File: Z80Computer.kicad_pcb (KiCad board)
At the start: 2 copper layers, 152.4 x 129.5 mm, 38 parts, among them IC1 Z80CPU, IC2_EEPROM1 28C256, IC6_SRAM1 KM62256CLP, J1 Conn_Coaxial_Power, J2 Conn_01x08_Pin, J3 Conn_01x08_Pin, SW1 SW_Push, U1 74LS244, U2 74LS32, U3 74LS273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

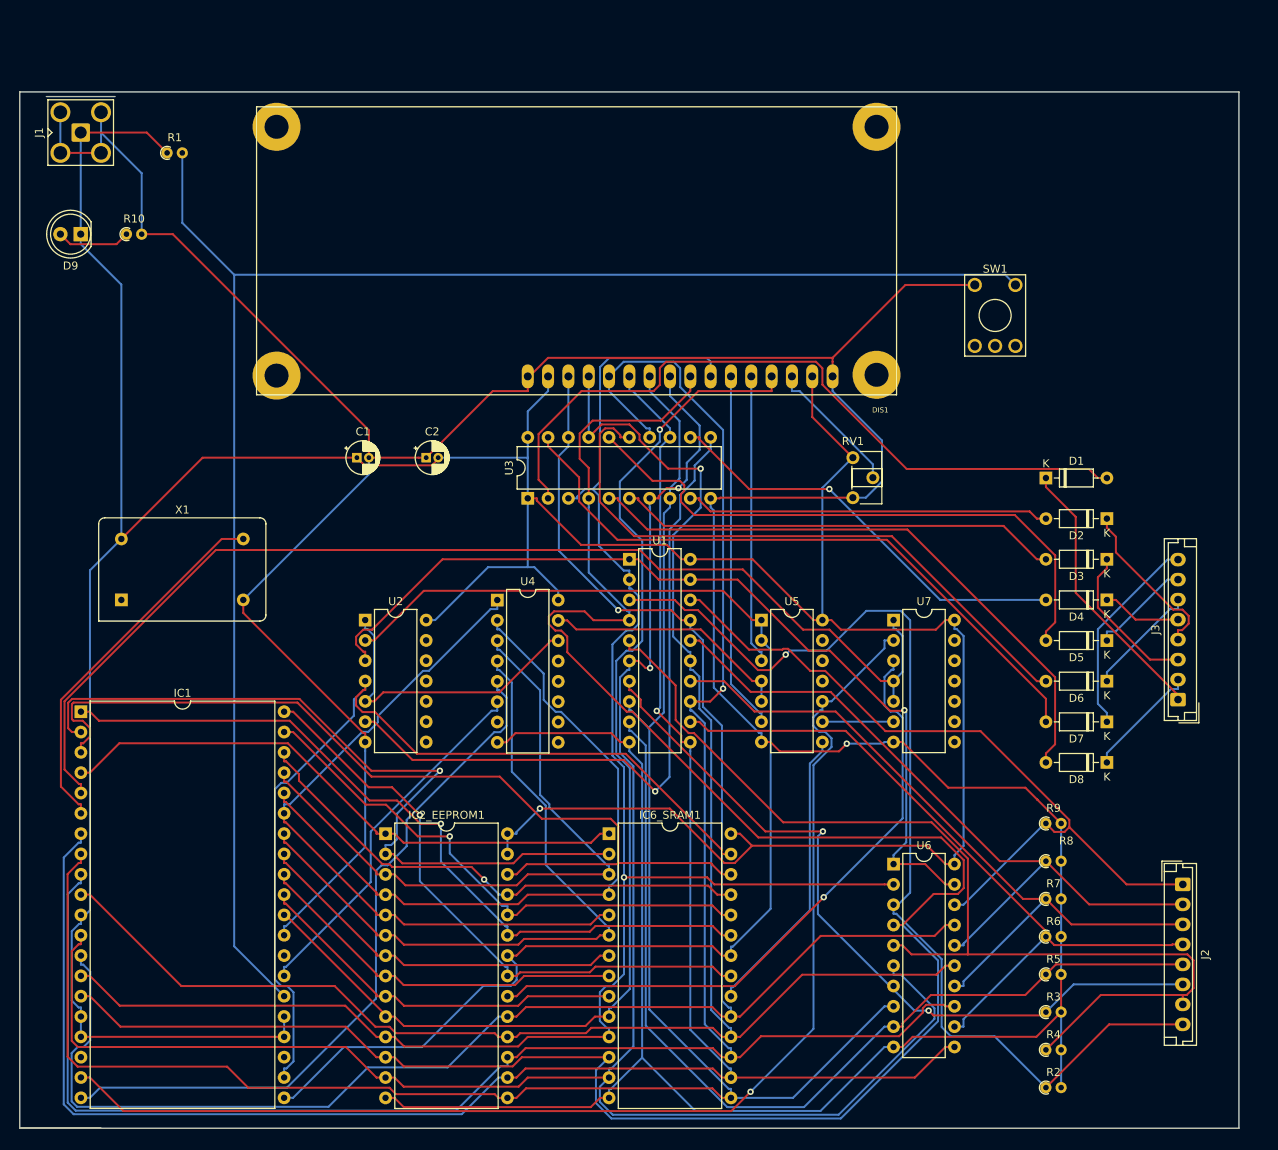
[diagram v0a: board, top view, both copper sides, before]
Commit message: reworked to correct z80 footprint
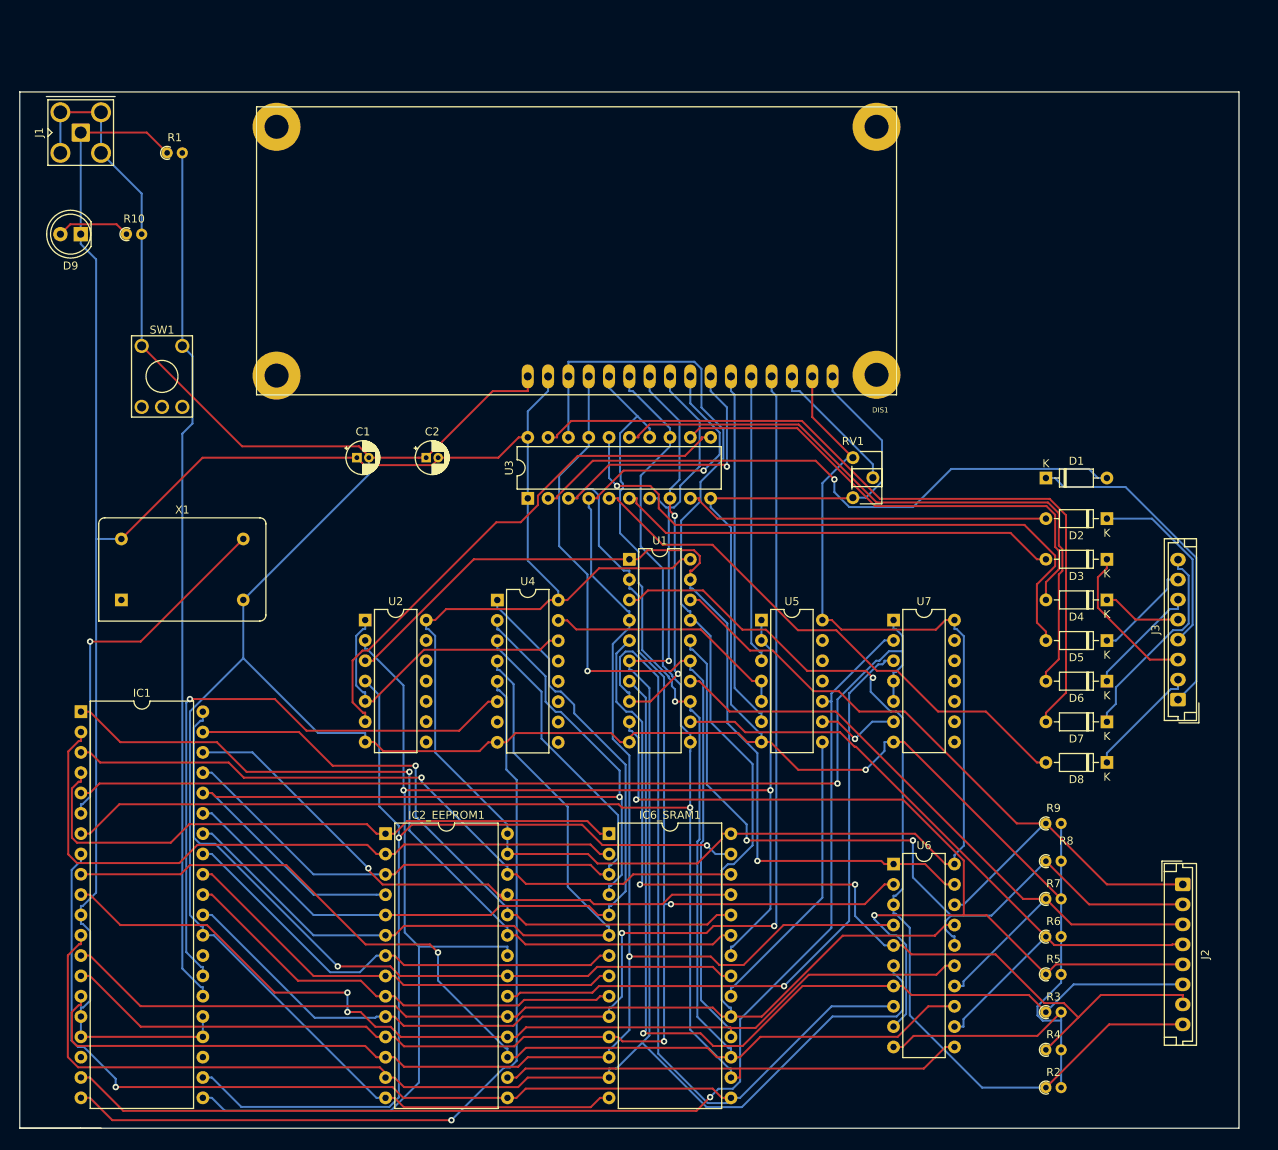
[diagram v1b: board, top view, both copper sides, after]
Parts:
- IC1: footprint Package_DIP:DIP-40_W25.4mm -> Package_DIP:DIP-40_W15.24mm
- moved SW1 104.4 mm to (63.5, 64.8)
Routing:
- net Net-(IC1-~{RESET}): track 208.9 -> 107.7 mm
- net /D1: track 275.2 -> 216.0 mm, vias 0 -> 2
- net Z80_PWRCAP: track 537.7 -> 485.0 mm
- net /D5: track 262.0 -> 224.4 mm, vias 1 -> 2
- net /A6: track 89.4 -> 122.4 mm, vias 0 -> 1
- net ~{M1}: track 45.9 -> 77.3 mm, vias 0 -> 1
- net /A13: track 116.8 -> 89.5 mm, vias 0 -> 1
- net ~{RD}: track 165.8 -> 190.0 mm, vias 0 -> 2
- net Net-(J2-Pin_6): track 96.7 -> 119.0 mm, vias 2 -> 1
- net Net-(U3-Cp): track 87.0 -> 65.6 mm, vias 1 -> 0
- net /A5: track 87.1 -> 104.6 mm
- net ~{IORQ}: track 90.0 -> 107.3 mm, vias 0 -> 1
- net Net-(D7-A): track 81.1 -> 97.5 mm
- net /A10: track 76.0 -> 91.6 mm
- net /D3: track 239.5 -> 254.8 mm, vias 0 -> 3
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
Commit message: Added RC reset and fixed RAM ROM chip select
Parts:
- added R11: 10K, Resistor_THT:R_Axial_DIN0204_L3.6mm_D1.6mm_P1.90mm_Vertical, F.Cu at (162.6, 92.1)
- added R12: 10K, Resistor_THT:R_Axial_DIN0204_L3.6mm_D1.6mm_P1.90mm_Vertical, F.Cu at (159.4, 92.1)
- added R13: 10K, Resistor_THT:R_Axial_DIN0204_L3.6mm_D1.6mm_P1.90mm_Vertical, F.Cu at (156.3, 92.1)
- added R14: 10K, Resistor_THT:R_Axial_DIN0204_L3.6mm_D1.6mm_P1.90mm_Vertical, F.Cu at (153.1, 92.1)
- moved R1 10.2 mm to (66.7, 50.8)
- moved J1 8.93 mm to (55.9, 47.0)
- moved D1 7.62 mm to (184.2, 81.3), turned to 180 degrees
- moved D9 7.62 mm to (55.9, 58.4)
- moved R10 5.08 mm to (61.6, 55.9)
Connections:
- D9 pad 1: +5V -> Net-(D9-K)
- D9 pad 2: Net-(D9-A) -> +5V
- R10 pad 1: Net-(D9-A) -> Net-(D9-K)
- U2 pad 10: unconnected-(U2-Pad10) -> +5V
- U2 pad 11: unconnected-(U2-Pad11) -> Net-(R11-Pad1)
- U2 pad 12: unconnected-(U2-Pad12) -> +5V
- U2 pad 13: unconnected-(U2-Pad13) -> +5V
- U2 pad 8: unconnected-(U2-Pad8) -> Net-(R12-Pad1)
- U2 pad 9: unconnected-(U2-Pad9) -> +5V
- U5 pad 10: ~{MREQ} -> MREQ
- U5 pad 11: unconnected-(U5-Pad11) -> Net-(R14-Pad1)
- U5 pad 12: unconnected-(U5-Pad12) -> +5V
- U5 pad 13: unconnected-(U5-Pad13) -> +5V
- U5 pad 9: Net-(U5-Pad9) -> /A15
- U7 pad 1: /A15 -> Net-(U7-Pad1)
- U7 pad 10: unconnected-(U7-Pad10) -> /A15
- U7 pad 11: unconnected-(U7-Pad11) -> Net-(R13-Pad1)
- U7 pad 12: unconnected-(U7-Pad12) -> +5V
- U7 pad 13: unconnected-(U7-Pad13) -> +5V
- U7 pad 2: ~{MREQ} -> MREQ
- U7 pad 4: /A15 -> ~{MREQ}
- U7 pad 5: /A15 -> ~{MREQ}
- U7 pad 6: Net-(U5-Pad9) -> MREQ
- U7 pad 8: unconnected-(U7-Pad8) -> Net-(U7-Pad1)
- U7 pad 9: unconnected-(U7-Pad9) -> /A15
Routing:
- net Net-(R12-Pad1): track 0.00 -> 123.0 mm, vias 0 -> 1
- net Net-(R11-Pad1): track 0.00 -> 82.6 mm, vias 0 -> 2
- net Net-(U7-Pad1): track 0.00 -> 47.4 mm
- net MREQ: track 0.00 -> 29.5 mm, vias 0 -> 4
- net /A15: track 127.6 -> 150.8 mm, vias 1 -> 3
- net Net-(R13-Pad1): track 0.00 -> 18.4 mm
- net Net-(R14-Pad1): track 0.00 -> 17.4 mm
- net Z80_PWRCAP: track 485.0 -> 497.1 mm, vias 1 -> 2
- net Net-(U5-Pad9): track 10.7 -> 0.00 mm, vias 1 -> 0
- net Net-(IC1-~{RESET}): track 107.7 -> 97.5 mm
- net Net-(D9-A): track 9.29 -> 0.00 mm
- net ~{MREQ}: track 150.5 -> 159.4 mm, vias 1 -> 2
- net Net-(D1-A): track 77.7 -> 69.1 mm
- net +5V: track 449.6 -> 457.5 mm
- net Net-(D1-K): track 41.6 -> 34.0 mm
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
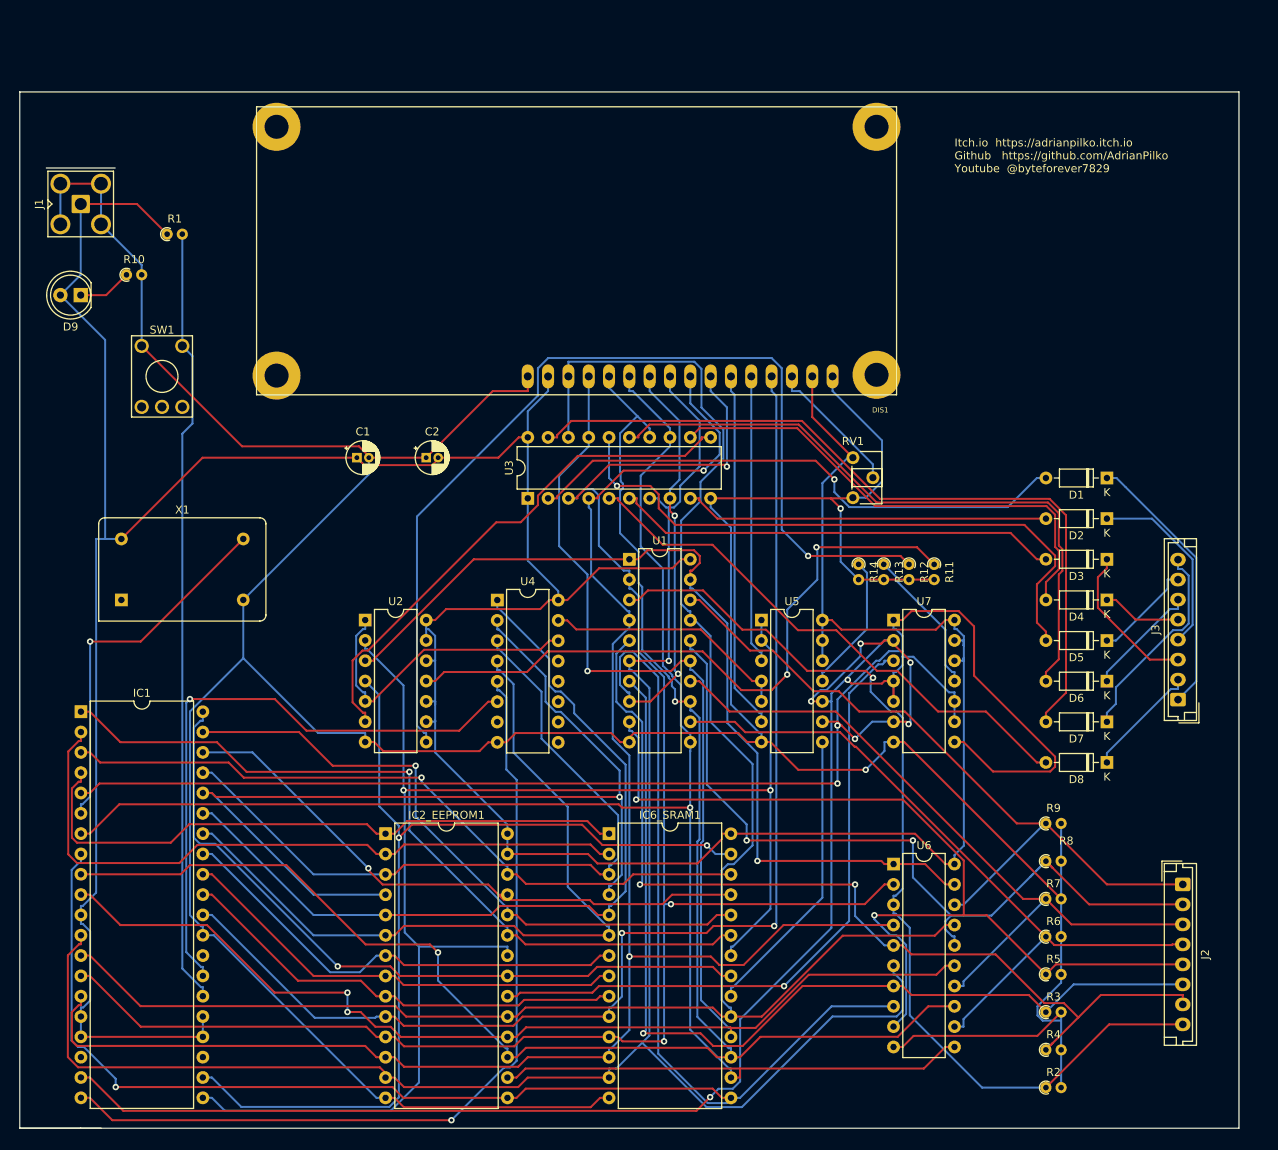
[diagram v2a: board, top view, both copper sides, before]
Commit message: added some footprints and updated pcb
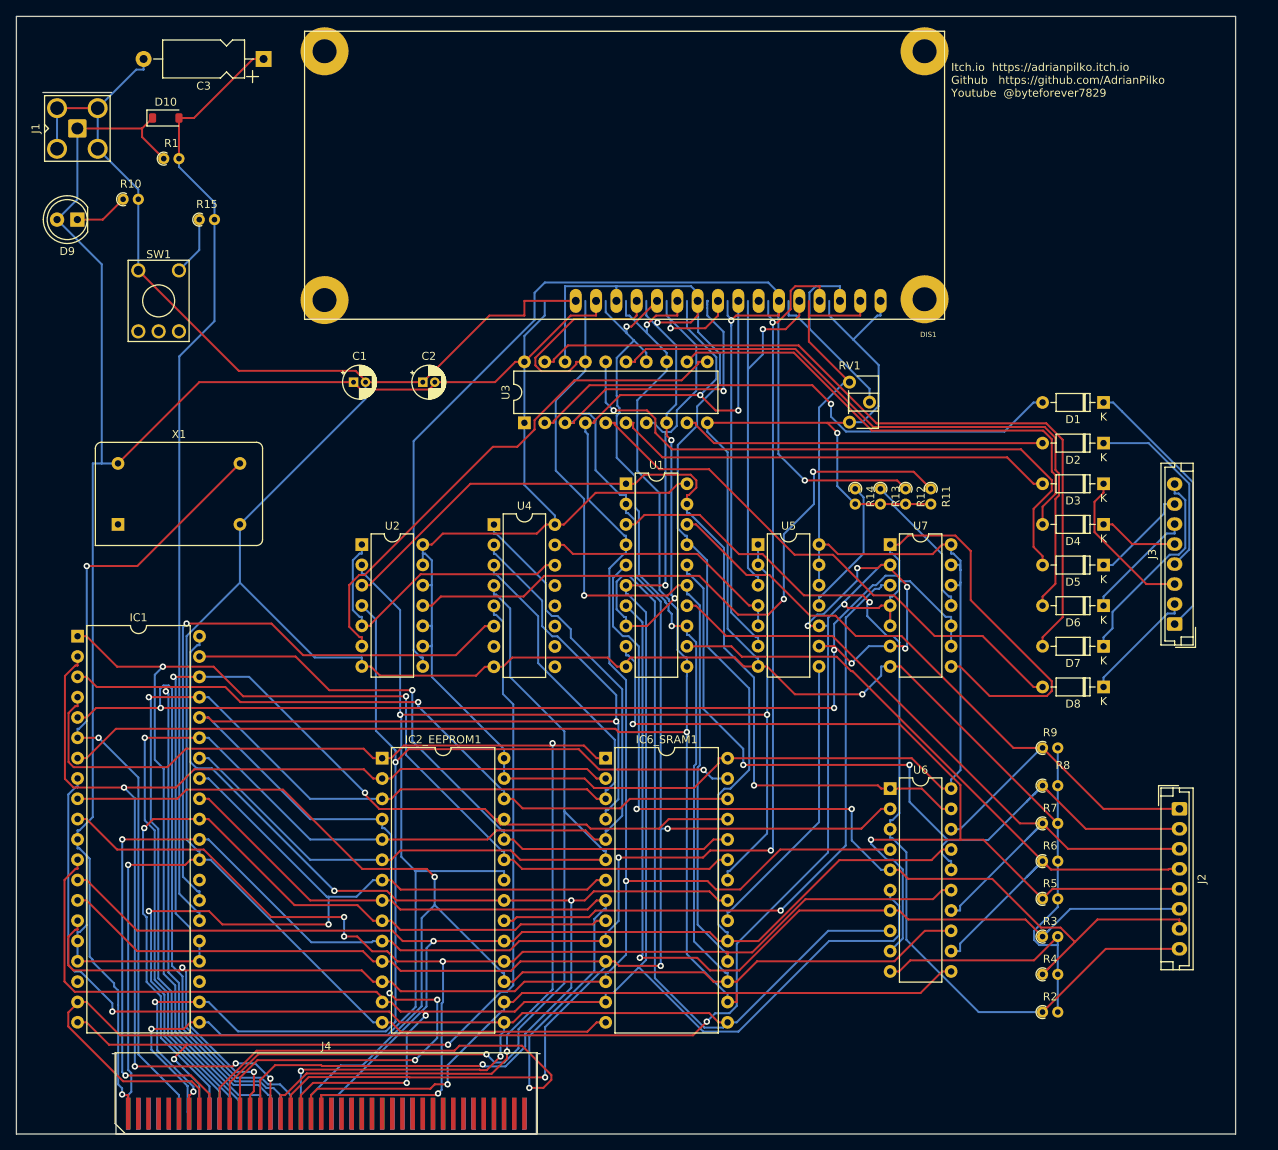
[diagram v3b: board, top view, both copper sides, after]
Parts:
- added C3: 1uF, Capacitor_THT:CP_Axial_L10.0mm_D4.5mm_P15.00mm_Horizontal, F.Cu at (78.7, 28.9)
- added D10: 1N4148W, Diode_SMD:D_SOD-123, F.Cu at (66.5, 36.3)
- added J4: Conn_01x40_Pin, Connector_PCBEdge:Samtec_MECF-40-0_-NP-L-DV_2x40_P1.27mm_Edge, F.Cu at (86.6, 158.2)
- added R15: 100R, Resistor_THT:R_Axial_DIN0204_L3.6mm_D1.6mm_P1.90mm_Vertical, F.Cu at (70.7, 49.0)
- moved DIS1 11.2 mm to (163.9, 61.4)
- moved D6 9.45 mm to (183.7, 97.2)
- moved D7 9.45 mm to (183.7, 102.3)
- moved J2 9.45 mm to (193.2, 122.6)
- moved U2 9.45 mm to (91.0, 89.6)
- moved U4 9.45 mm to (107.5, 87.1)
- moved U5 9.45 mm to (140.6, 89.6)
- moved U7 9.45 mm to (157.1, 89.6)
- moved D9 9.45 mm to (55.5, 49.0)
- moved R10 9.45 mm to (61.2, 46.4)
- moved C1 9.45 mm to (90.0, 69.3)
- moved C2 9.45 mm to (98.6, 69.3)
- moved D1 9.45 mm to (183.7, 71.8)
- moved D2 9.45 mm to (183.7, 76.9)
- moved D3 9.45 mm to (183.7, 82.0)
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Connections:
- IC1 pad 26: Net-(IC1-~{RESET}) -> Net-(D10-A)
- R1 pad 2: Net-(IC1-~{RESET}) -> Net-(D10-A)
- SW1 pad 2: Net-(IC1-~{RESET}) -> Net-(R15-Pad1)
- U2 pad 11: Net-(R11-Pad1) -> unconnected-(U2-Pad11)
- U2 pad 8: Net-(R12-Pad1) -> unconnected-(U2-Pad8)
- U5 pad 11: Net-(R14-Pad1) -> unconnected-(U5-Pad11)
- U7 pad 11: Net-(R13-Pad1) -> unconnected-(U7-Pad11)
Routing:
- net Net-(D10-A): track 0.00 -> 118.8 mm
- net Net-(IC1-~{RESET}): track 97.5 -> 0.00 mm
- net /A2: track 57.0 -> 136.7 mm, vias 0 -> 1
- net /A14: track 78.9 -> 153.6 mm, vias 0 -> 2
- net /A4: track 97.4 -> 172.0 mm, vias 0 -> 1
- net /A15: track 150.8 -> 216.5 mm, vias 3 -> 4
- net /A6: track 122.4 -> 187.2 mm, vias 1 -> 4
- net /A0: track 156.8 -> 221.1 mm, vias 2 -> 5
- net /A8: track 75.6 -> 139.2 mm, vias 1 -> 3
- net /A11: track 98.7 -> 162.1 mm, vias 1 -> 2
- net /A7: track 93.3 -> 156.4 mm, vias 0 -> 1
- net Z80_PWRCAP: track 497.1 -> 559.7 mm, vias 2 -> 3
- net /A13: track 89.5 -> 150.2 mm, vias 1 -> 2
- net /A10: track 91.6 -> 151.6 mm, vias 1 -> 3
- net +5V: track 457.5 -> 516.2 mm, vias 0 -> 1
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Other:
- board size 152.4 x 129.5 mm -> 152.4 x 139.7 mm
